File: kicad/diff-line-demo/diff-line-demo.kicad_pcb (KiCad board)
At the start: 4 copper layers, 0 parts

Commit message: Butterfly slot using Inkscape + DXF import (thanks to Petr Dvořák for the tip).
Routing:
- added copper zone on In1.Cu, net (none)
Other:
- board outline added: 120 x 120 mm
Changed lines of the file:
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@@
 		(capping no)
 		(filling no)
-		(zone_defaults)
 		(pcbplotparams
 			(layerselection 0x00000000_00000000_55555555_5755f5ff)
@@
 		)
 	)
+	(gr_rect
+		(start 90 40)
+		(end 210 160)
+		(stroke
+			(width 0.05)
+			(type solid)
+		)
+		(fill no)
+		(layer "Edge.Cuts")
+	)
+	(zone
+		(layers "F.Cu" "B.Cu" "In1.Cu" "In2.Cu" "Edge.Cuts")
+		(hatch edge 0.5)
+		(connect_pads
+			(clearance 0)
+		)
+		(min_thickness 0.25)
+		(keepout
+			(tracks not_allowed)
+			(vias not_allowed)
+			(pads not_allowed)
+			(copperpour not_allowed)
+			(footprints allowed)
+		)
+		(placement
+			(enabled no)
+			(sheetname "")
+		)
+		(fill
+			(thermal_gap 0.5)
+			(thermal_bridge_width 0.5)
+			(island_removal_mode 0)
+		)
+		(polygon
+			(pts
+				(xy 185.355343 140.07375) (xy 183.55872 141.783469) (xy 181.687893 143.395186) (xy 179.746962 144.907204)
+				(xy 177.740024 146.317825) (xy 175.671178 147.625352) (xy 173.544521 148.828086) (xy 171.364152 149.924331)
+				(xy 169.134169 150.912389) (xy 166.858671 151.790562) (xy 164.541755 152.557153) (xy 162.18752 153.210464)
+				(xy 159.800064 153.748798) (xy 157.383486 154.170457) (xy 154.941883 154.473744) (xy 152.479353 154.656961)
+				(xy 149.999995 154.71841) (xy 147.520638 154.656962) (xy 145.058108 154.473745) (xy 142.616505 154.170459)
+				(xy 140.199926 153.7488) (xy 137.81247 153.210466) (xy 135.458235 152.557154) (xy 133.141319 151.790564)
+				(xy 130.86582 150.91239) (xy 128.635838 149.924332) (xy 126.455469 148.828087) (xy 124.328813 147.625352)
+				(xy 122.259967 146.317826) (xy 120.25303 144.907204) (xy 118.3121 143.395186) (xy 116.441275 141.783469)
+				(xy 114.644653 140.07375) (xy 150 104.718411)
+			)
+		)
+	)
+	(zone
+		(layers "F.Cu" "B.Cu" "In1.Cu" "In2.Cu" "Edge.Cuts")
+		(hatch edge 0.5)
+		(connect_pads
+			(clearance 0)
+		)
+		(min_thickness 0.25)
+		(keepout
+			(tracks not_allowed)
+			(vias not_allowed)
+			(pads not_allowed)
+			(copperpour not_allowed)
+			(footprints allowed)
+		)
+		(placement
+			(enabled no)
+			(sheetname "")
+		)
+		(fill
+			(thermal_gap 0.5)
+			(thermal_bridge_width 0.5)
+			(island_removal_mode 0)
+		)
+		(polygon
+			(pts
+				(xy 145.25 100) (xy 109.894661 135.355347) (xy 108.184942 133.558725) (xy 106.573224 131.6879) (xy 105.061206 129.746969)
+				(xy 103.650585 127.740032) (xy 102.343058 125.671186) (xy 101.140323 123.544529) (xy 100.044078 121.36416)
+				(xy 99.05602 119.134177) (xy 98.177847 116.858679) (xy 97.411256 114.541763) (xy 96.757945 112.187528)
+				(xy 96.219611 109.800072) (xy 95.797952 107.383493) (xy 95.494665 104.941889) (xy 95.311449 102.47936)
+				(xy 95.25 100.000002) (xy 95.31145 97.520645) (xy 95.494666 95.058115) (xy 95.797953 92.616512)
+				(xy 96.219612 90.199933) (xy 96.757946 87.812477) (xy 97.411258 85.458242) (xy 98.177849 83.141327)
+				(xy 99.056022 80.865829) (xy 100.044079 78.635846) (xy 101.140324 76.455477) (xy 102.343059 74.328821)
+				(xy 103.650585 72.259975) (xy 105.061206 70.253037) (xy 106.573224 68.312106) (xy 108.184942 66.44128)
+				(xy 109.894661 64.644657)
+			)
+		)
+	)
+	(zone
+		(layers "F.Cu" "B.Cu" "In1.Cu" "In2.Cu" "Edge.Cuts")
+		(hatch edge 0.5)
+		(connect_pads
+			(clearance 0)
+		)
+		(min_thickness 0.25)
+		(keepout
+			(tracks not_allowed)
+			(vias not_allowed)
+			(pads not_allowed)
+			(copperpour not_allowed)
+			(footprints allowed)
+		)
+		(placement
+			(enabled no)
+			(sheetname "")
+		)
+		(fill
+			(thermal_gap 0.5)
+			(thermal_bridge_width 0.5)
+			(island_removal_mode 0)
+		)
+		(polygon
+			(pts
+				(xy 154.968411 100.218411) (xy 145.031589 100.218411) (xy 145.031589 99.781589) (xy 154.968411 99.781589)
+			)
+		)
+	)
+	(zone
+		(layers "F.Cu" "B.Cu" "In1.Cu" "In2.Cu" "Edge.Cuts")
+		(hatch edge 0.5)
+		(connect_pads
+			(clearance 0)
+		)
+		(min_thickness 0.25)
+		(keepout
+			(tracks not_allowed)
+			(vias not_allowed)
+			(pads not_allowed)
+			(copperpour not_allowed)
+			(footprints allowed)
+		)
+		(placement
+			(enabled no)
+			(sheetname "")
+		)
+		(fill
+			(thermal_gap 0.5)
+			(thermal_bridge_width 0.5)
+			(island_removal_mode 0)
+		)
+		(polygon
+			(pts
+				(xy 152.479358 45.27986) (xy 154.941888 45.463077) (xy 157.383491 45.766364) (xy 159.800069 46.188023)
+				(xy 162.187525 46.726357) (xy 164.54176 47.379668) (xy 166.858676 48.146259) (xy 169.134174 49.024432)
+				(xy 171.364156 50.01249) (xy 173.544524 51.108735) (xy 175.671181 52.311469) (xy 177.740027 53.618996)
+				(xy 179.746964 55.029617) (xy 181.687895 56.541635) (xy 183.55872 58.153352) (xy 185.355343 59.863071)
+				(xy 150 95.218411) (xy 114.644653 59.863071) (xy 116.441275 58.153352) (xy 118.312101 56.541635)
+				(xy 120.253032 55.029616) (xy 122.25997 53.618995) (xy 124.328816 52.311468) (xy 126.455473 51.108734)
+				(xy 128.635842 50.012489) (xy 130.865825 49.024431) (xy 133.141323 48.146257) (xy 135.458239 47.379666)
+				(xy 137.812475 46.726355) (xy 140.199931 46.188021) (xy 142.61651 45.766362) (xy 145.058113 45.463076)
+				(xy 147.520643 45.279859) (xy 150 45.21841)
+			)
+		)
+	)
+	(zone
+		(layers "F.Cu" "B.Cu" "In1.Cu" "In2.Cu" "Edge.Cuts")
+		(hatch edge 0.5)
+		(connect_pads
+			(clearance 0)
+		)
+		(min_thickness 0.25)
+		(keepout
+			(tracks not_allowed)
+			(vias not_allowed)
+			(pads not_allowed)
+			(copperpour not_allowed)
+			(footprints allowed)
+		)
+		(placement
+			(enabled no)
+			(sheetname "")
+		)
+		(fill
+			(thermal_gap 0.5)
+			(thermal_bridge_width 0.5)
+			(island_removal_mode 0)
+		)
+		(polygon
+			(pts
+				(xy 191.815058 66.44128) (xy 193.426776 68.312106) (xy 194.938794 70.253037) (xy 196.349415 72.259975)
+				(xy 197.656941 74.328821) (xy 198.859676 76.455477) (xy 199.955921 78.635846) (xy 200.943978 80.865829)
+				(xy 201.822151 83.141327) (xy 202.588742 85.458242) (xy 203.242054 87.812477) (xy 203.780388 90.199933)
+				(xy 204.202047 92.616512) (xy 204.505334 95.058115) (xy 204.68855 97.520645) (xy 204.75 100.000002)
+				(xy 204.688551 102.47936) (xy 204.505335 104.941889) (xy 204.202048 107.383493) (xy 203.780389 109.800072)
+				(xy 203.242055 112.187528) (xy 202.588744 114.541763) (xy 201.822153 116.858679) (xy 200.94398 119.134177)
+				(xy 199.955922 121.36416) (xy 198.859677 123.544529) (xy 197.656942 125.671186) (xy 196.349415 127.740032)
+				(xy 194.938794 129.746969) (xy 193.426776 131.6879) (xy 191.815058 133.558725) (xy 190.105339 135.355347)
+				(xy 154.75 100) (xy 190.105339 64.644657)
+			)
+		)
+	)
+	(zone
+		(layers "F.Cu" "B.Cu" "In1.Cu" "In2.Cu" "Edge.Cuts")
+		(hatch edge 0.5)
+		(connect_pads
+			(clearance 0)
+		)
+		(min_thickness 0.25)
+		(keepout
+			(tracks not_allowed)
+			(vias not_allowed)
+			(pads not_allowed)
+			(copperpour not_allowed)
+			(footprints allowed)
+		)
+		(placement
+			(enabled no)
+			(sheetname "")
+		)
+		(fill
+			(thermal_gap 0.5)
+			(thermal_bridge_width 0.5)
+			(island_removal_mode 0)
+		)
+		(polygon
+			(pts
+				(xy 150.218411 104.936823) (xy 149.781588 104.936823) (xy 149.781589 95) (xy 150.218412 95)
+			)
+		)
+	)
+	(zone
+		(layer "In1.Cu")
+		(hatch edge 0.5)
+		(connect_pads
+			(clearance 0.5)
+		)
+		(min_thickness 0.25)
+		(fill yes
+			(thermal_gap 0.5)
+			(thermal_bridge_width 0.5)
+			(island_removal_mode 1)
+		)
+		(polygon
+			(pts
+				(xy 90 40) (xy 210 40) (xy 210 160) (xy 90 160)
+			)
+		)
+	)

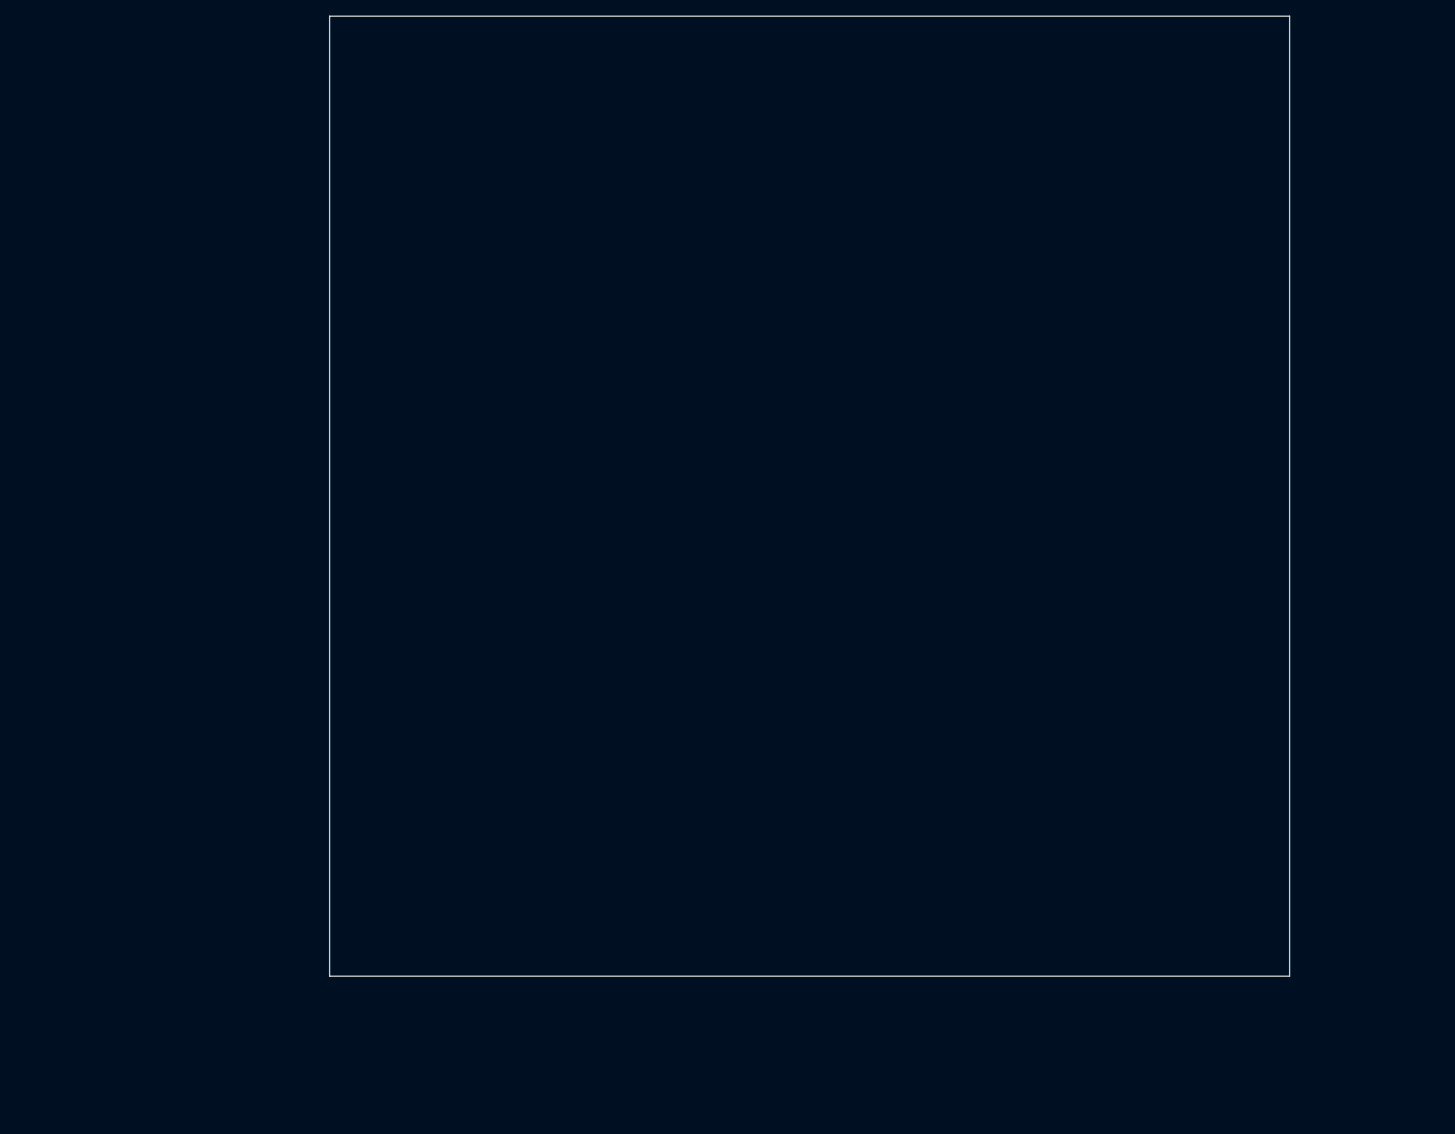
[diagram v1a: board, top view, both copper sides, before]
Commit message: Fix layers of the ground plane and slots.
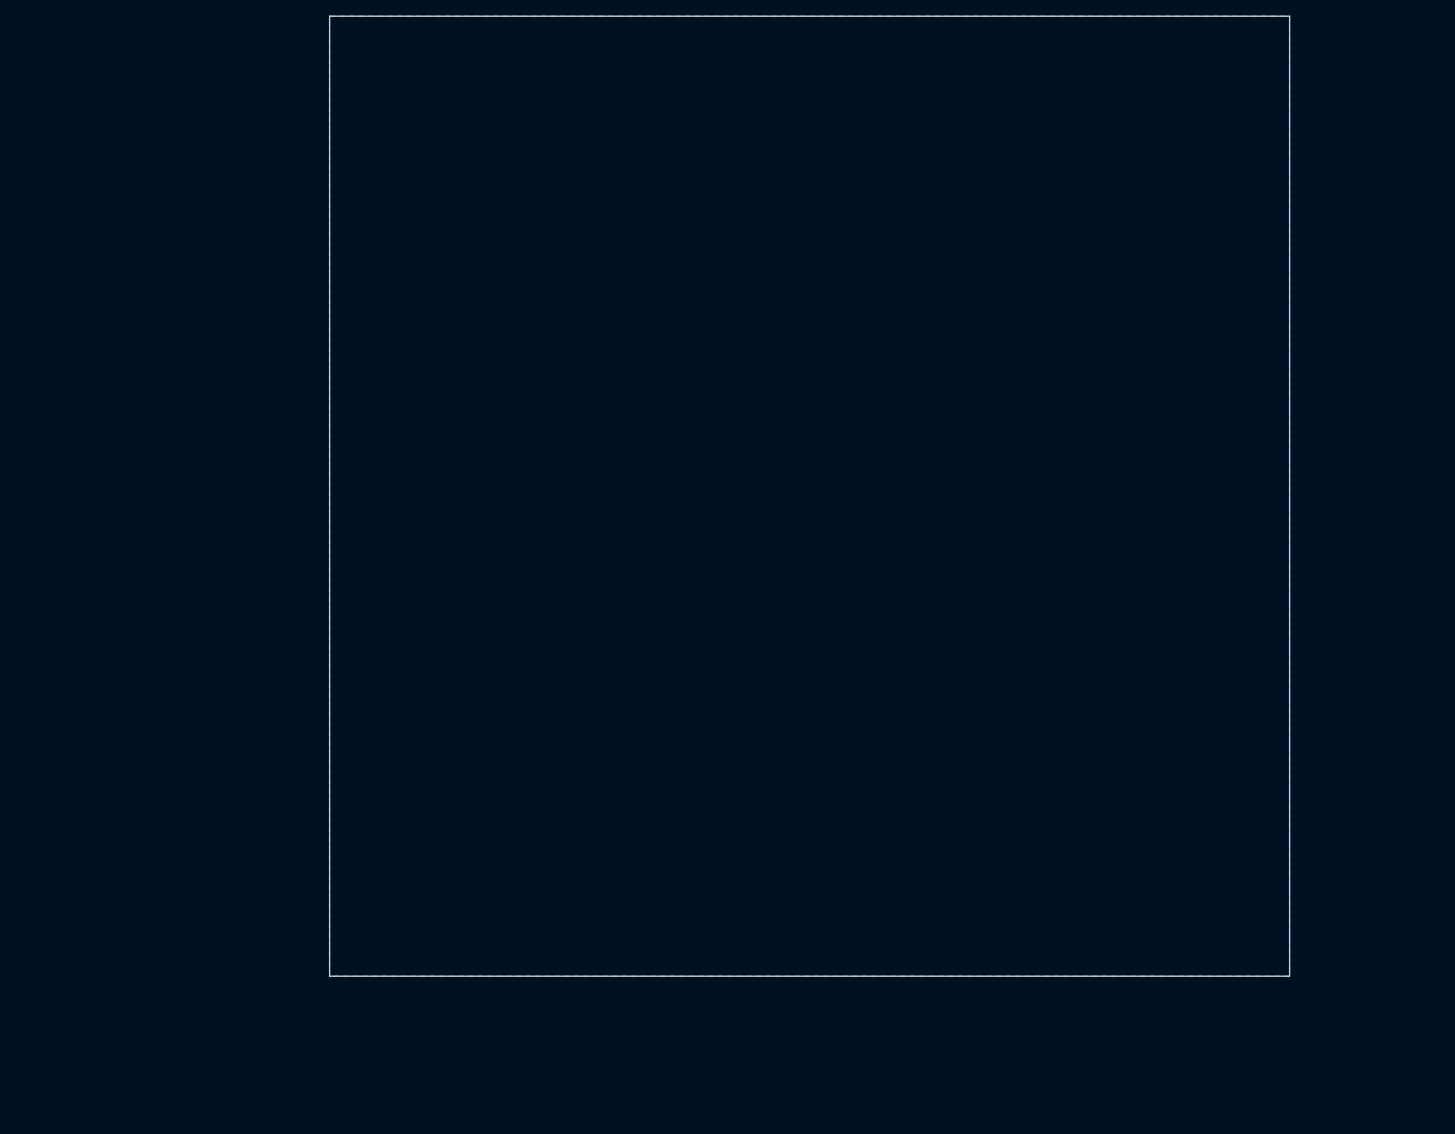
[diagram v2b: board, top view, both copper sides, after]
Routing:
- added copper zone on B.Cu, net (none)
- added copper zone on In2.Cu, net (none)
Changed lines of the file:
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@@
 	)
 	(zone
-		(layer "In1.Cu")
+		(layers "B.Cu" "In1.Cu" "In2.Cu")
 		(hatch edge 0.5)
 		(connect_pads

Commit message: HDMI connectors selection, begin of PCB.
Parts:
- added J1: HDMI_A, Connector_Video:HDMI_A_Amphenol_10029449-x01xLF_Horizontal, F.Cu at (213.0, 99.7)
- added J2: HDMI_A, Connector_Video:HDMI_A_Amphenol_10029449-x01xLF_Horizontal, F.Cu at (86.7, 100.3)
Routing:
- net Net-(J1-D2+): track 0.00 -> 202.3 mm
- net Net-(J1-D2-): track 0.00 -> 201.9 mm
